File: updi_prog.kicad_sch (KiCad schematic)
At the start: 17 parts, among them J1 UPDI, P1 USB_B, U1 LM1117-3.3, U2 FT232RL

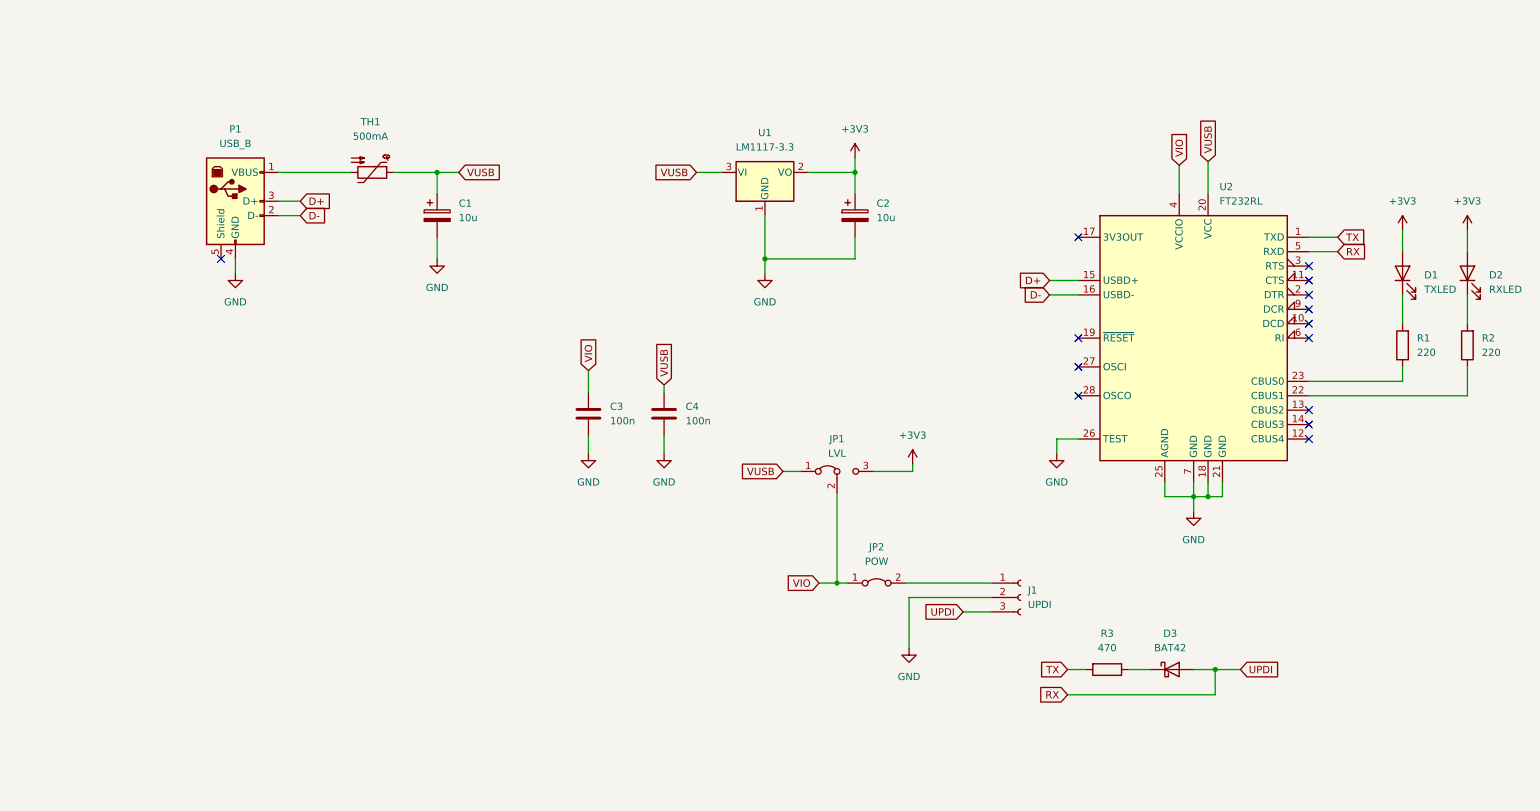
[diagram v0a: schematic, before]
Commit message: added power led
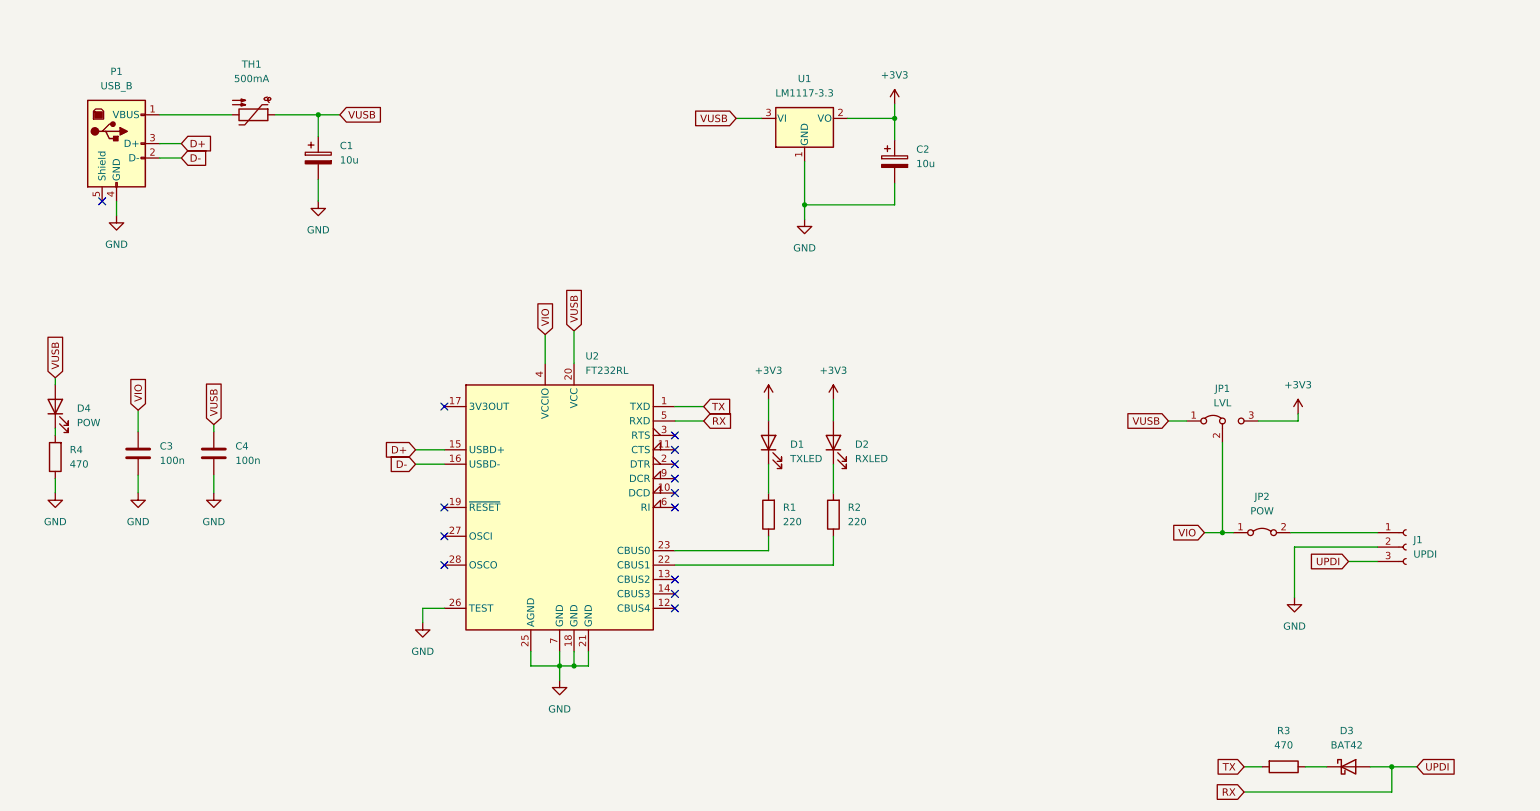
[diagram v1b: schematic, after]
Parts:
- added D4: POW, LED_THT:LED_D3.0mm_Clear, symbol device:LED
- added R4: 470, Resistor_THT:R_Axial_DIN0207_L6.3mm_D2.5mm_P10.16mm_Horizontal, symbol device:R
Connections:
- net GND: now also R4.1
- net VUSB: now also D4.2 (A)
- new net: D4.1 (K), R4.2
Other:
- moved on the sheet: C1, C2, C3, C4, D1, D2, D3, J1, JP1, JP2, P1, R1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

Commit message: smaller pcb
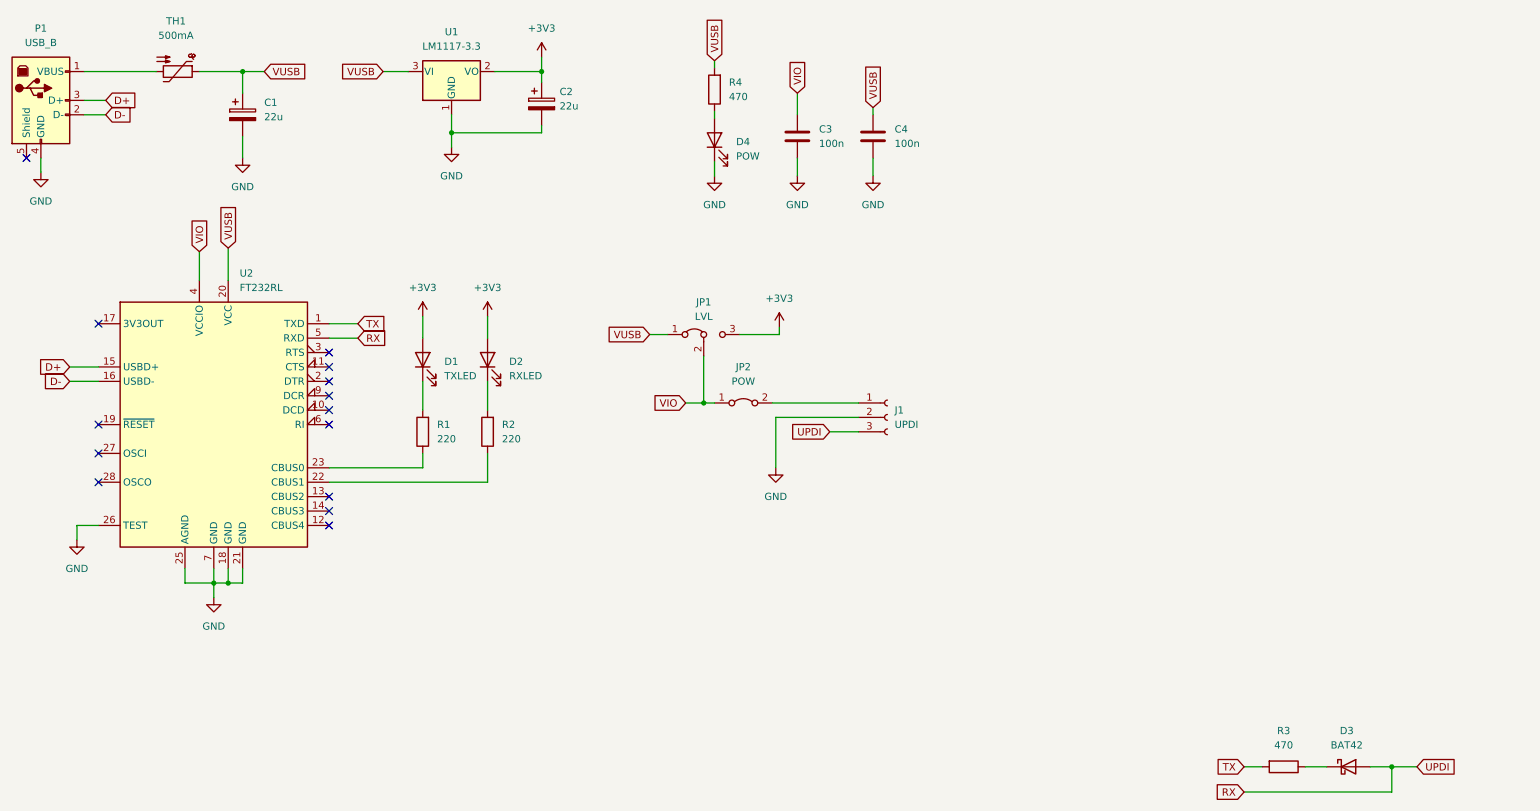
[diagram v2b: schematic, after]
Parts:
- C1, C2: value 10u -> 22u
- C3, C4: footprint Capacitor_THT:C_Disc_D4.3mm_W1.9mm_P5.00mm -> Capacitor_SMD:C_1206_3216Metric_Pad1.33x1.80mm_HandSolder
- R1, R2, R3, R4: footprint Resistor_THT:R_Axial_DIN0207_L6.3mm_D2.5mm_P10.16mm_Horizontal -> Resistor_SMD:R_1206_3216Metric_Pad1.30x1.75mm_HandSolder
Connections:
- net GND: now also D4.1 (K); no longer R4.1
- net VUSB: now also R4.2; no longer D4.2 (A)
- new net: D4.2 (A), R4.1
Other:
- moved on the sheet: C1, C2, C3, C4, D1, D2, D4, J1, JP1, JP2, P1, R1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

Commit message: changed connector to standard AVR-UPDI
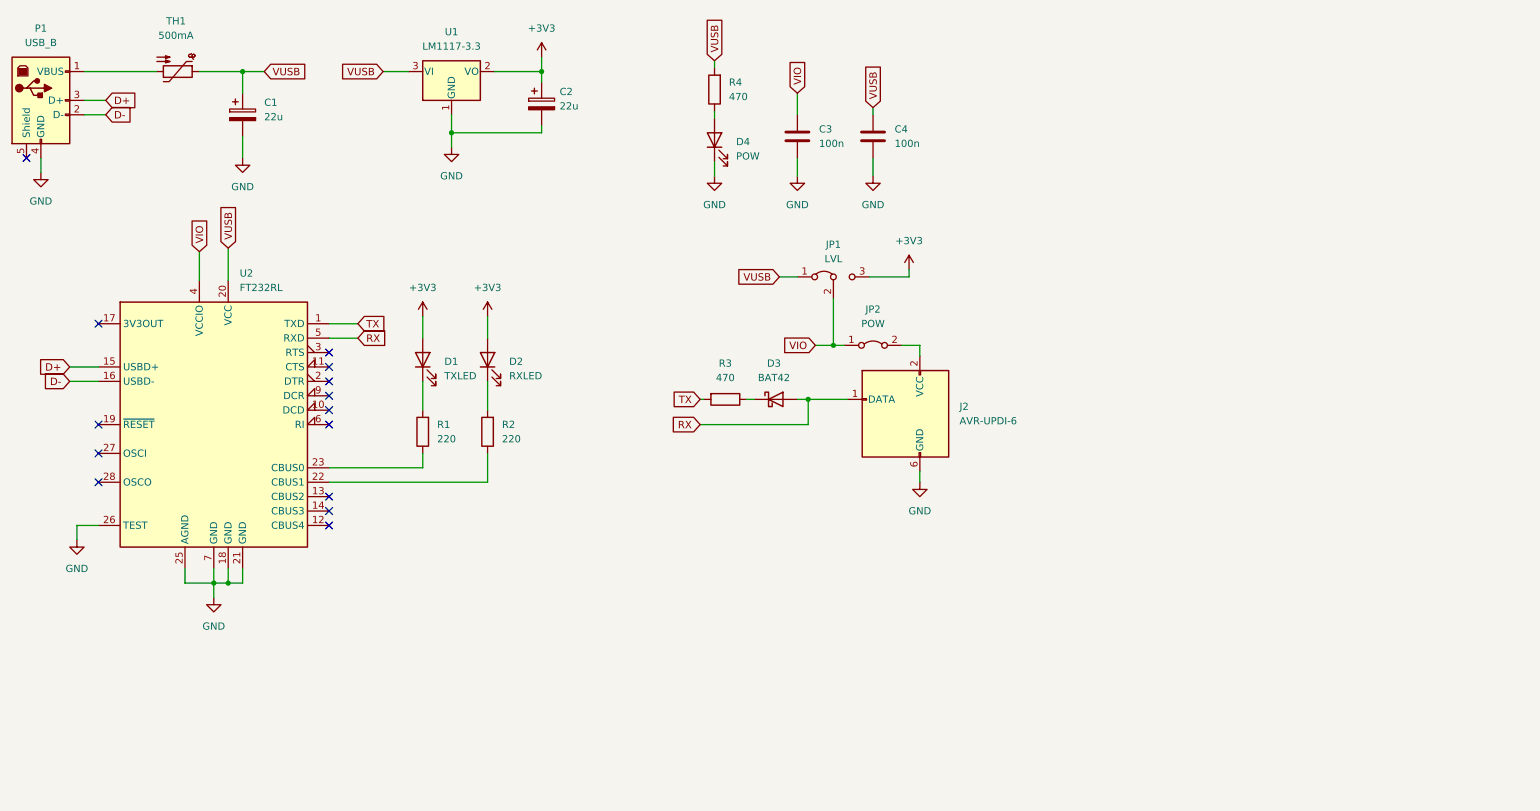
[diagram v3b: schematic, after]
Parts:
- removed J1: UPDI, Connector_PinHeader_2.54mm:PinHeader_1x03_P2.54mm_Vertical, symbol connector:Conn_01x03_Female
- added J2: AVR-UPDI-6, Connector_PinHeader_2.54mm:PinHeader_2x03_P2.54mm_Vertical, symbol connector:AVR-UPDI-6
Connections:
- net GND: now also J2.6 (GND)
- net RX: now also J2.1 (DATA)
- net at JP2.2 (B): now also J2.2 (VCC)
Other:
- moved on the sheet: D3, JP1, JP2, R3
